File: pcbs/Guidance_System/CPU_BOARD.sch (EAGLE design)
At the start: 16 parts, among them J1 22-27-2081-08, J2 22-27-2021-02, J3 22-05-7048-04, J4 22-05-7048-04, J5 22-27-2081-08, J6 22-27-2021-02, J7 22-27-2081-08

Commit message: * Added Driver board. Many corrections and refinements.
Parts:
- removed S1: 2P2T, switch:2P2T
- added J10, J11, J12, J13, J14: 22-27-2081-08, con-molex:22-27-2081-08
- added J15, J16: 22-27-2041-04, con-molex:22-27-2041-04
- added J17, J8, J9: 22-27-2021-02, con-molex:22-27-2021-02
- J3, J4: value 22-05-7048-04 -> 22-27-2041-04; device con-molex:22-05-7048-04 -> con-molex:22-27-2041-04
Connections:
- new net N$19: J13-5.S, J13-6.S
- new net N$24: J1-1.S, J3-2.S, J4-2.S, J9-1.S, U$1.GND@2
- new net N$26: J10-8.S, J14-8.S
- new net N$27: J10-7.S, J14-5.S
- new net N$28: J13-7.S, J14-6.S
- new net N$29: J13-8.S, J14-7.S
- new net N$31: J11-8.S, J12-8.S, J17-2.S
- new net N$32: J10-3.S, J11-2.S, J12-2.S, J13-3.S, J14-1.S
- new net N$33: J11-1.S, J12-1.S, J14-2.S
- new net N$34: J11-7.S, J12-7.S, J17-1.S
- new net N$35: J10-1.S, J13-1.S, J14-4.S
- new net N$37: J11-6.S, J15-1.S
- new net N$38: J11-5.S, J15-2.S
- new net N$39: J11-4.S, J15-3.S
- new net N$40: J11-3.S, J15-4.S
- new net N$41: J12-6.S, J16-1.S
- new net N$42: J12-5.S, J16-2.S
- new net N$43: J12-4.S, J16-3.S
- new net N$44: J12-3.S, J16-4.S
- net N$4: now also J10-5.S, J10-6.S; no longer J1-1.S, J3-2.S, J4-2.S, U$1.GND@2
- net N$5: now also J8-2.S; no longer S1.3.2
- net VCC: now also J8-1.S, J9-2.S; no longer S1.3.1
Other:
- note added: "S1 Driver"
- note added: "S2 Driver"

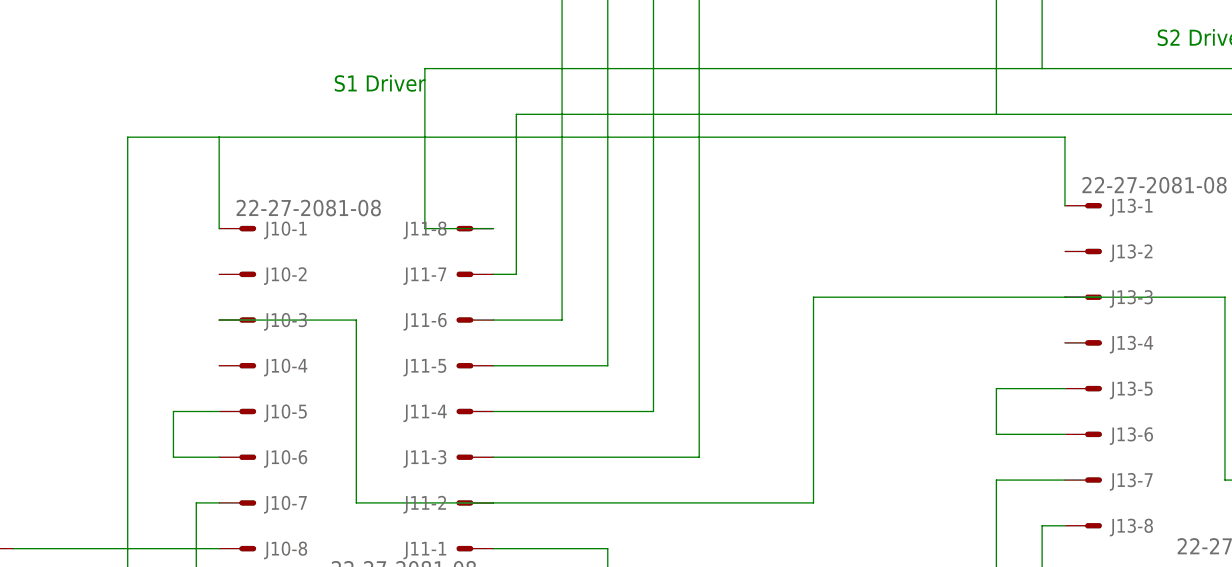
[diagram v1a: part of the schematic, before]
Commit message: * Flipped power/switch around * Adding holes /tracks for step control pins on drivers * Adding text in and around pcb components to help us identify different parts
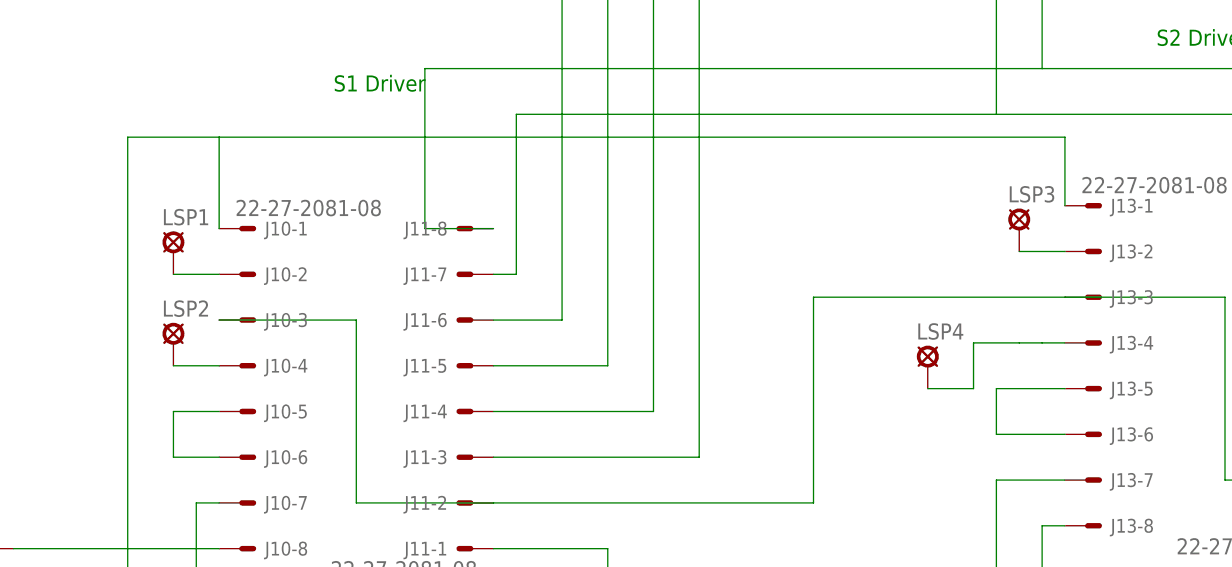
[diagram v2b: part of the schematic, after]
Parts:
- added LSP1, LSP2, LSP3, LSP4: LSP10, solpad:LSP10
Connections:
- new net N$25: J10-4.S, LSP2.MP
- new net N$30: J10-2.S, LSP1.MP
- new net N$36: J13-4.S, LSP4.MP
- new net N$45: J13-2.S, LSP3.MP
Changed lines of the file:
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@@
 <part name="J16" library="con-molex" deviceset="22-?-04" device="27-2041"/>
 <part name="J17" library="con-molex" deviceset="22-?-02" device="27-2021"/>
+<part name="LSP1" library="solpad" deviceset="LSP10" device=""/>
+<part name="LSP2" library="solpad" deviceset="LSP10" device=""/>
+<part name="LSP3" library="solpad" deviceset="LSP10" device=""/>
+<part name="LSP4" library="solpad" deviceset="LSP10" device=""/>
 </parts>
 <sheets>
@@
 <instance part="J17" gate="-1" x="-15.24" y="215.9" rot="R90"/>
 <instance part="J17" gate="-2" x="-10.16" y="215.9" rot="R90"/>
+<instance part="LSP1" gate="1" x="-106.68" y="182.88"/>
+<instance part="LSP2" gate="1" x="-106.68" y="172.72"/>
+<instance part="LSP3" gate="1" x="-12.7" y="185.42"/>
+<instance part="LSP4" gate="1" x="-22.86" y="170.18"/>
 </instances>
 <busses>
@@
 </segment>
 </net>
+<net name="N$25" class="0">
+<segment>
+<pinref part="J10" gate="-4" pin="S"/>
+<wire x1="-101.6" y1="170.18" x2="-106.68" y2="170.18" width="0.1524" layer="91"/>
+<pinref part="LSP2" gate="1" pin="MP"/>
+</segment>
+</net>
+<net name="N$30" class="0">
+<segment>
+<pinref part="J10" gate="-2" pin="S"/>
+<wire x1="-101.6" y1="180.34" x2="-106.68" y2="180.34" width="0.1524" layer="91"/>
+<pinref part="LSP1" gate="1" pin="MP"/>
+</segment>
+</net>
+<net name="N$36" class="0">
+<segment>
+<pinref part="J13" gate="-4" pin="S"/>
+<wire x1="-7.62" y1="172.72" x2="-10.16" y2="172.72" width="0.1524" layer="91"/>
+<pinref part="LSP4" gate="1" pin="MP"/>
+<wire x1="-10.16" y1="172.72" x2="-12.7" y2="172.72" width="0.1524" layer="91"/>
+<wire x1="-22.86" y1="167.64" x2="-17.78" y2="167.64" width="0.1524" layer="91"/>
+<wire x1="-17.78" y1="167.64" x2="-17.78" y2="172.72" width="0.1524" layer="91"/>
+<wire x1="-17.78" y1="172.72" x2="-12.7" y2="172.72" width="0.1524" layer="91"/>
+</segment>
+</net>
+<net name="N$45" class="0">
+<segment>
+<pinref part="J13" gate="-2" pin="S"/>
+<wire x1="-7.62" y1="182.88" x2="-12.7" y2="182.88" width="0.1524" layer="91"/>
+<pinref part="LSP3" gate="1" pin="MP"/>
+</segment>
+</net>

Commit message: * Minor adjustments
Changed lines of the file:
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@@
 <wire x1="12.7" y1="88.9" x2="12.7" y2="86.36" width="0.1524" layer="91"/>
 <wire x1="12.7" y1="86.36" x2="33.02" y2="86.36" width="0.1524" layer="91"/>
+<junction x="33.02" y="86.36"/>
 </segment>
 </net>
@@
 <wire x1="-10.16" y1="203.2" x2="-78.74" y2="203.2" width="0.1524" layer="91"/>
 <wire x1="-10.16" y1="213.36" x2="-10.16" y2="203.2" width="0.1524" layer="91"/>
+<junction x="-10.16" y="203.2"/>
 </segment>
 </net>
@@
 <pinref part="J17" gate="-1" pin="S"/>
 <wire x1="-15.24" y1="213.36" x2="-15.24" y2="198.12" width="0.1524" layer="91"/>
+<junction x="-15.24" y="198.12"/>
 </segment>
 </net>
@@
 <wire x1="-101.6" y1="195.58" x2="-101.6" y2="185.42" width="0.1524" layer="91"/>
 <wire x1="-111.76" y1="195.58" x2="-101.6" y2="195.58" width="0.1524" layer="91"/>
-</segment>
-</net>
+<junction x="-101.6" y="195.58"/>
+</segment>
+</net>

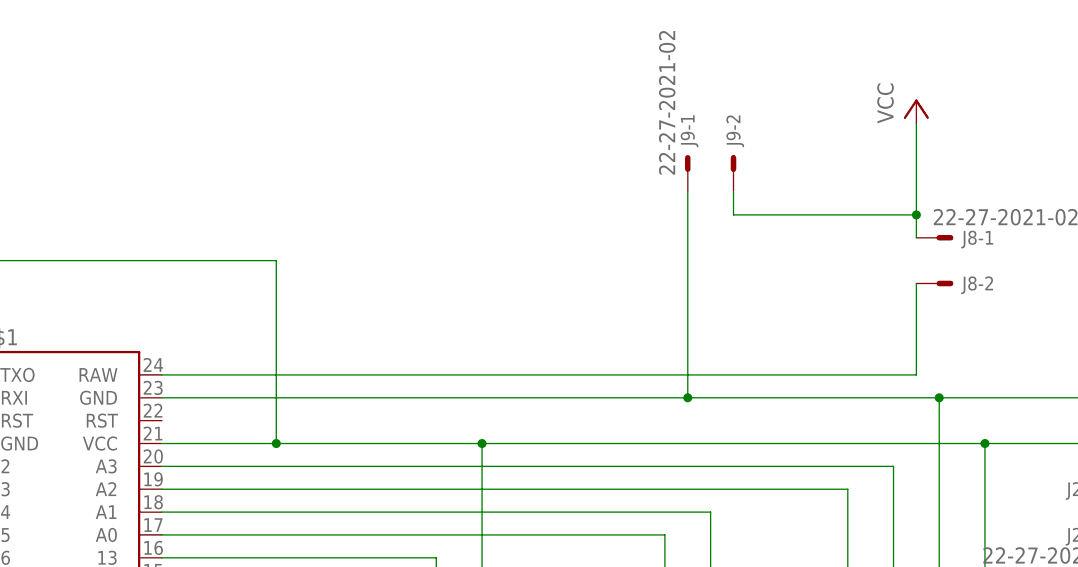
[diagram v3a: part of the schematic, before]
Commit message: * Adding in resistors, so we can measure voltage of battery at some point.
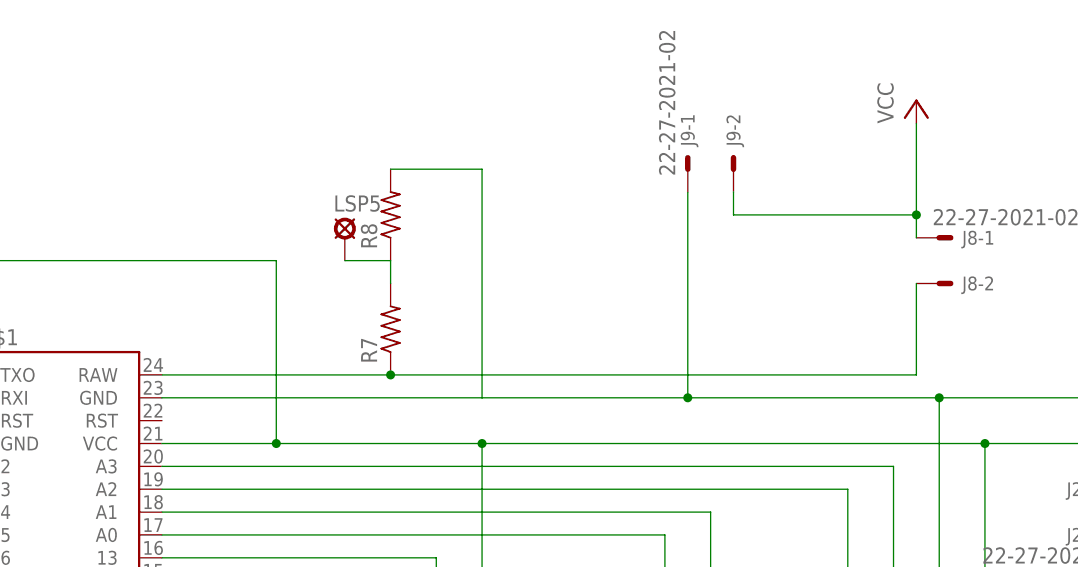
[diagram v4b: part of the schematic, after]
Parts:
- added LSP5: LSP11, solpad:LSP11
- added R7, R8: (no value), rcl:R-US_0204/5
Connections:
- new net N$47: LSP5.MP, R7.2, R8.1
- net N$24: now also R8.2
- net N$5: now also R7.1
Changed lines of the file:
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@@
 <part name="LSP3" library="solpad" deviceset="LSP10" device=""/>
 <part name="LSP4" library="solpad" deviceset="LSP10" device=""/>
+<part name="R7" library="rcl" deviceset="R-US_" device="0204/5"/>
+<part name="R8" library="rcl" deviceset="R-US_" device="0204/5"/>
+<part name="LSP5" library="solpad" deviceset="LSP11" device=""/>
 </parts>
 <sheets>
@@
 <instance part="LSP3" gate="1" x="-12.7" y="185.42"/>
 <instance part="LSP4" gate="1" x="-22.86" y="170.18"/>
+<instance part="R7" gate="G$1" x="-25.4" y="73.66" rot="R90"/>
+<instance part="R8" gate="G$1" x="-25.4" y="86.36" rot="R90"/>
+<instance part="LSP5" gate="1" x="-30.48" y="83.82"/>
 </instances>
 <busses>
@@
 <segment>
 <pinref part="U$1" gate="G$1" pin="RAW"/>
-<wire x1="-50.8" y1="68.58" x2="33.02" y2="68.58" width="0.1524" layer="91"/>
+<wire x1="-50.8" y1="68.58" x2="-25.4" y2="68.58" width="0.1524" layer="91"/>
+<wire x1="-25.4" y1="68.58" x2="33.02" y2="68.58" width="0.1524" layer="91"/>
 <wire x1="33.02" y1="68.58" x2="33.02" y2="78.74" width="0.1524" layer="91"/>
 <pinref part="J8" gate="-2" pin="S"/>
+<pinref part="R7" gate="G$1" pin="1"/>
+<junction x="-25.4" y="68.58"/>
 </segment>
 </net>
@@
 <pinref part="J3" gate="-2" pin="S"/>
 <wire x1="35.56" y1="66.04" x2="7.62" y2="66.04" width="0.1524" layer="91"/>
-<wire x1="7.62" y1="66.04" x2="-50.8" y2="66.04" width="0.1524" layer="91"/>
+<wire x1="7.62" y1="66.04" x2="-15.24" y2="66.04" width="0.1524" layer="91"/>
+<wire x1="-15.24" y1="66.04" x2="-50.8" y2="66.04" width="0.1524" layer="91"/>
 <wire x1="15.24" y1="7.62" x2="15.24" y2="27.94" width="0.1524" layer="91"/>
 <wire x1="15.24" y1="27.94" x2="35.56" y2="27.94" width="0.1524" layer="91"/>
@@
 <wire x1="7.62" y1="88.9" x2="7.62" y2="66.04" width="0.1524" layer="91"/>
 <junction x="7.62" y="66.04"/>
+<pinref part="R8" gate="G$1" pin="2"/>
+<wire x1="-25.4" y1="91.44" x2="-15.24" y2="91.44" width="0.1524" layer="91"/>
+<wire x1="-15.24" y1="91.44" x2="-15.24" y2="66.04" width="0.1524" layer="91"/>
 </segment>
 </net>
@@
 </segment>
 </net>
+<net name="N$47" class="0">
+<segment>
+<pinref part="R7" gate="G$1" pin="2"/>
+<pinref part="R8" gate="G$1" pin="1"/>
+<wire x1="-25.4" y1="78.74" x2="-25.4" y2="81.28" width="0.1524" layer="91"/>
+<wire x1="-25.4" y1="81.28" x2="-30.48" y2="81.28" width="0.1524" layer="91"/>
+<pinref part="LSP5" gate="1" pin="MP"/>
+</segment>
+</net>

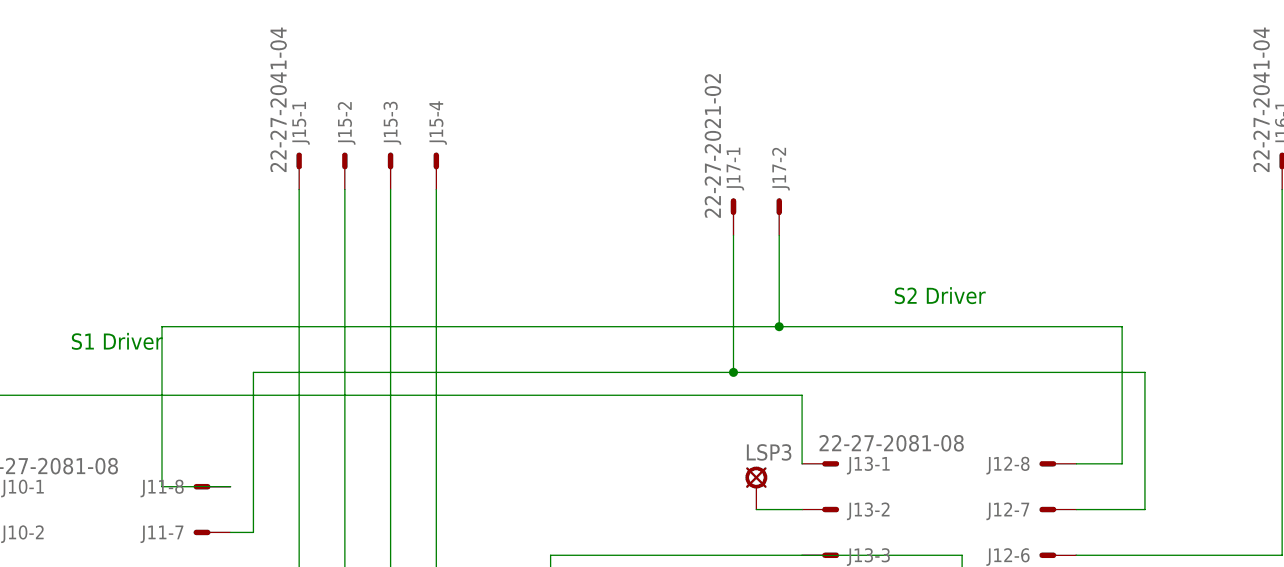
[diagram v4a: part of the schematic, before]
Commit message: * Added in capacitor
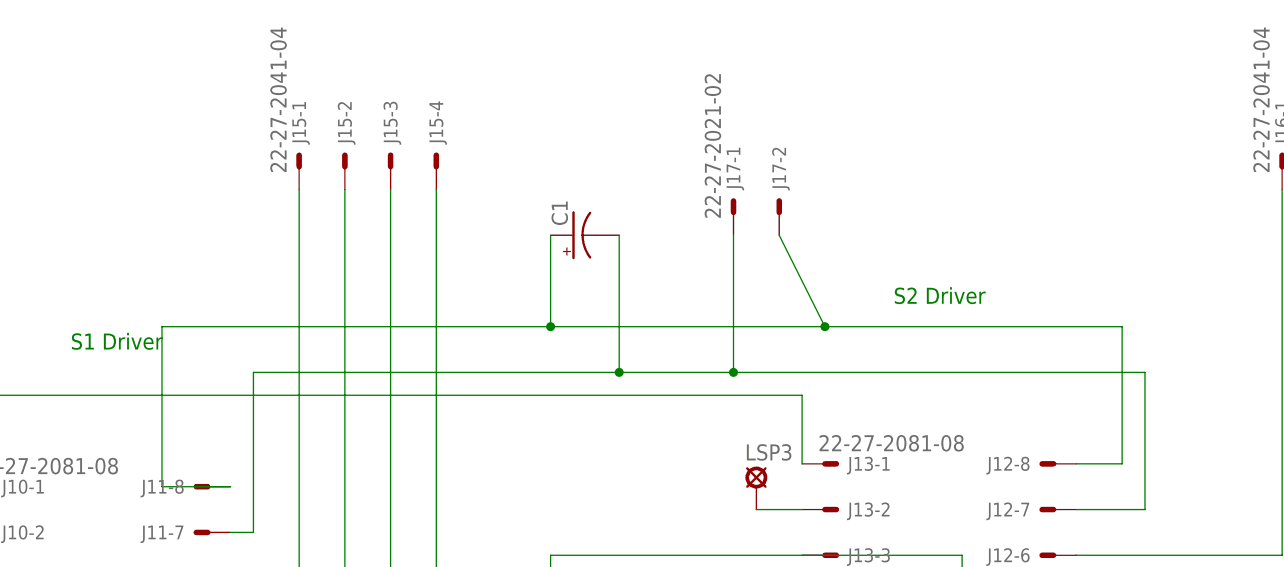
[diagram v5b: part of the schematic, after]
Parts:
- added C1: (no value), resistor:CPOL-USE2.5-7
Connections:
- net N$31: now also C1.+
- net N$34: now also C1.-
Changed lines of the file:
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@@
 <part name="R8" library="rcl" deviceset="R-US_" device="0204/5"/>
 <part name="LSP5" library="solpad" deviceset="LSP11" device=""/>
+<part name="C1" library="resistor" deviceset="CPOL-US" device="E2.5-7"/>
 </parts>
 <sheets>
@@
 <instance part="R8" gate="G$1" x="-25.4" y="86.36" rot="R90"/>
 <instance part="LSP5" gate="1" x="-30.48" y="83.82"/>
+<instance part="C1" gate="G$1" x="-33.02" y="213.36" rot="R90"/>
 </instances>
 <busses>
@@
 <wire x1="22.86" y1="187.96" x2="27.94" y2="187.96" width="0.1524" layer="91"/>
 <wire x1="27.94" y1="187.96" x2="27.94" y2="203.2" width="0.1524" layer="91"/>
-<wire x1="27.94" y1="203.2" x2="-10.16" y2="203.2" width="0.1524" layer="91"/>
+<wire x1="27.94" y1="203.2" x2="-5.08" y2="203.2" width="0.1524" layer="91"/>
 <pinref part="J17" gate="-2" pin="S"/>
-<wire x1="-10.16" y1="203.2" x2="-78.74" y2="203.2" width="0.1524" layer="91"/>
-<wire x1="-10.16" y1="213.36" x2="-10.16" y2="203.2" width="0.1524" layer="91"/>
-<junction x="-10.16" y="203.2"/>
+<wire x1="-5.08" y1="203.2" x2="-35.56" y2="203.2" width="0.1524" layer="91"/>
+<wire x1="-35.56" y1="203.2" x2="-78.74" y2="203.2" width="0.1524" layer="91"/>
+<wire x1="-10.16" y1="213.36" x2="-5.08" y2="203.2" width="0.1524" layer="91"/>
+<junction x="-5.08" y="203.2"/>
+<pinref part="C1" gate="G$1" pin="+"/>
+<wire x1="-35.56" y1="203.2" x2="-35.56" y2="213.36" width="0.1524" layer="91"/>
+<junction x="-35.56" y="203.2"/>
 </segment>
 </net>
@@
 <wire x1="-71.12" y1="180.34" x2="-68.58" y2="180.34" width="0.1524" layer="91"/>
 <wire x1="-68.58" y1="180.34" x2="-68.58" y2="198.12" width="0.1524" layer="91"/>
-<wire x1="-68.58" y1="198.12" x2="-15.24" y2="198.12" width="0.1524" layer="91"/>
+<wire x1="-68.58" y1="198.12" x2="-27.94" y2="198.12" width="0.1524" layer="91"/>
 <pinref part="J12" gate="-7" pin="S"/>
+<wire x1="-27.94" y1="198.12" x2="-15.24" y2="198.12" width="0.1524" layer="91"/>
 <wire x1="-15.24" y1="198.12" x2="30.48" y2="198.12" width="0.1524" layer="91"/>
 <wire x1="22.86" y1="182.88" x2="30.48" y2="182.88" width="0.1524" layer="91"/>
@@
 <wire x1="-15.24" y1="213.36" x2="-15.24" y2="198.12" width="0.1524" layer="91"/>
 <junction x="-15.24" y="198.12"/>
-</segment>
-</net>
+<pinref part="C1" gate="G$1" pin="-"/>
+<wire x1="-27.94" y1="213.36" x2="-27.94" y2="198.12" width="0.1524" layer="91"/>
+<junction x="-27.94" y="198.12"/>
+</segment>
+</net>
